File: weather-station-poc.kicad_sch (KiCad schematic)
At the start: 0 parts

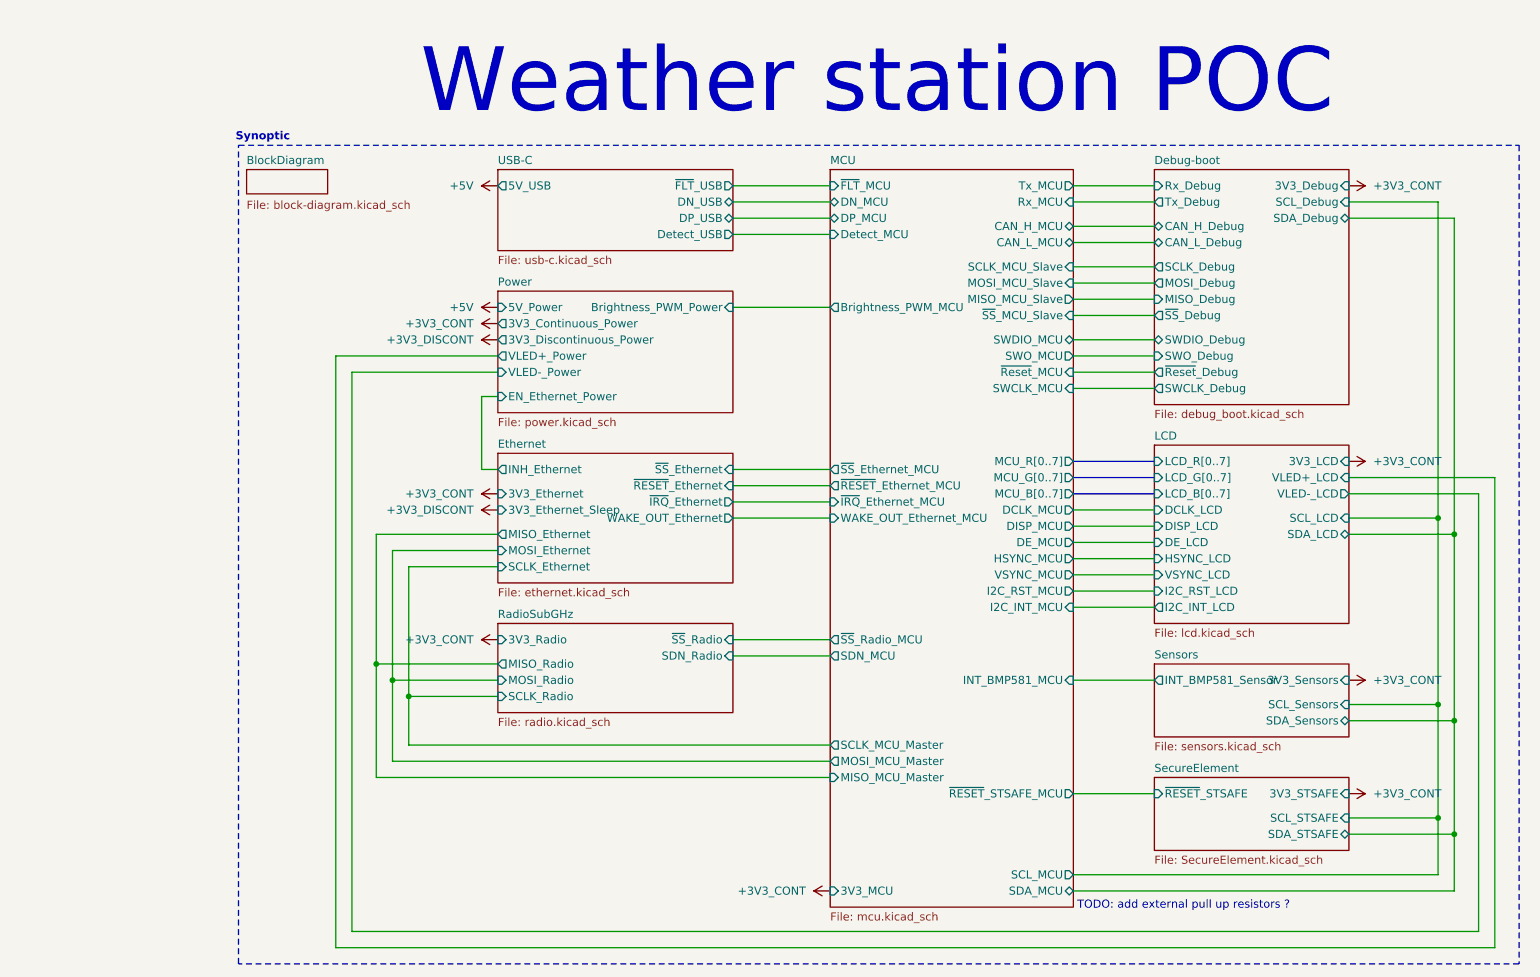
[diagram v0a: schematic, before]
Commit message: Remove Ethernet part, critical error, LAN8651 is 10BASE-T1S !
10BASE-T1S is not suitable with RJ45 connector and not connectable to computer
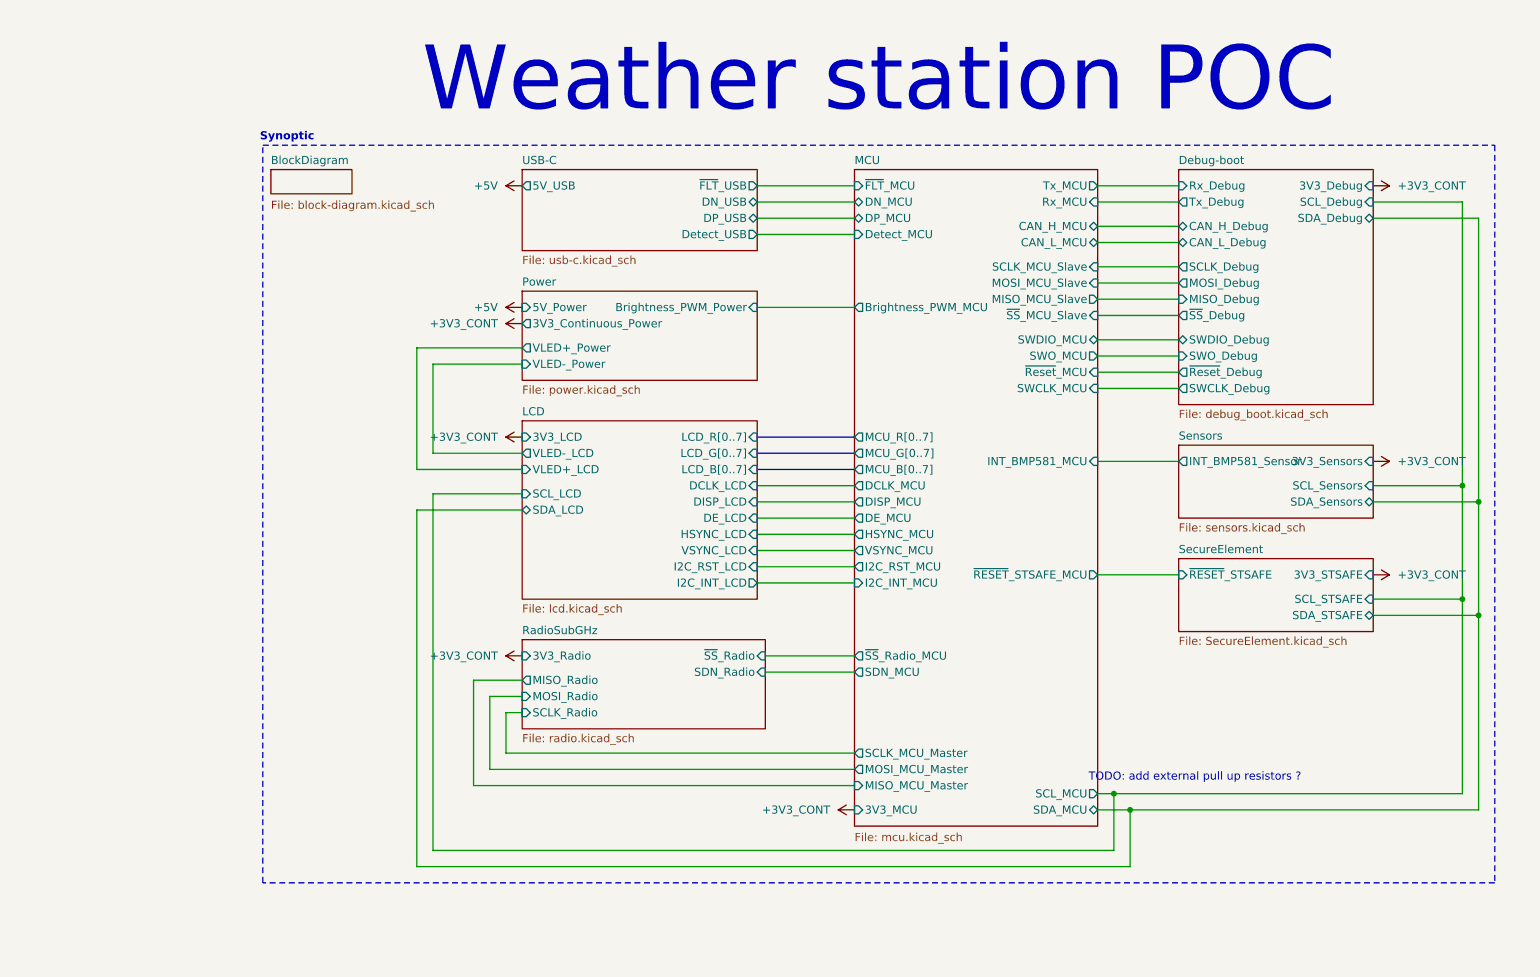
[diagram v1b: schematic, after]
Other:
- removed sheet Ethernet
- sheet MCU ports: added none; removed WAKE_OUT_Ethernet_MCU, ~{IRQ}_Ethernet_MCU, ~{RESET}_Ethernet_MCU, ~{SS}_Ethernet_MCU
- sheet Power ports: added none; removed 3V3_Discontinuous_Power, EN_Ethernet_Power

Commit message: Reorder components number
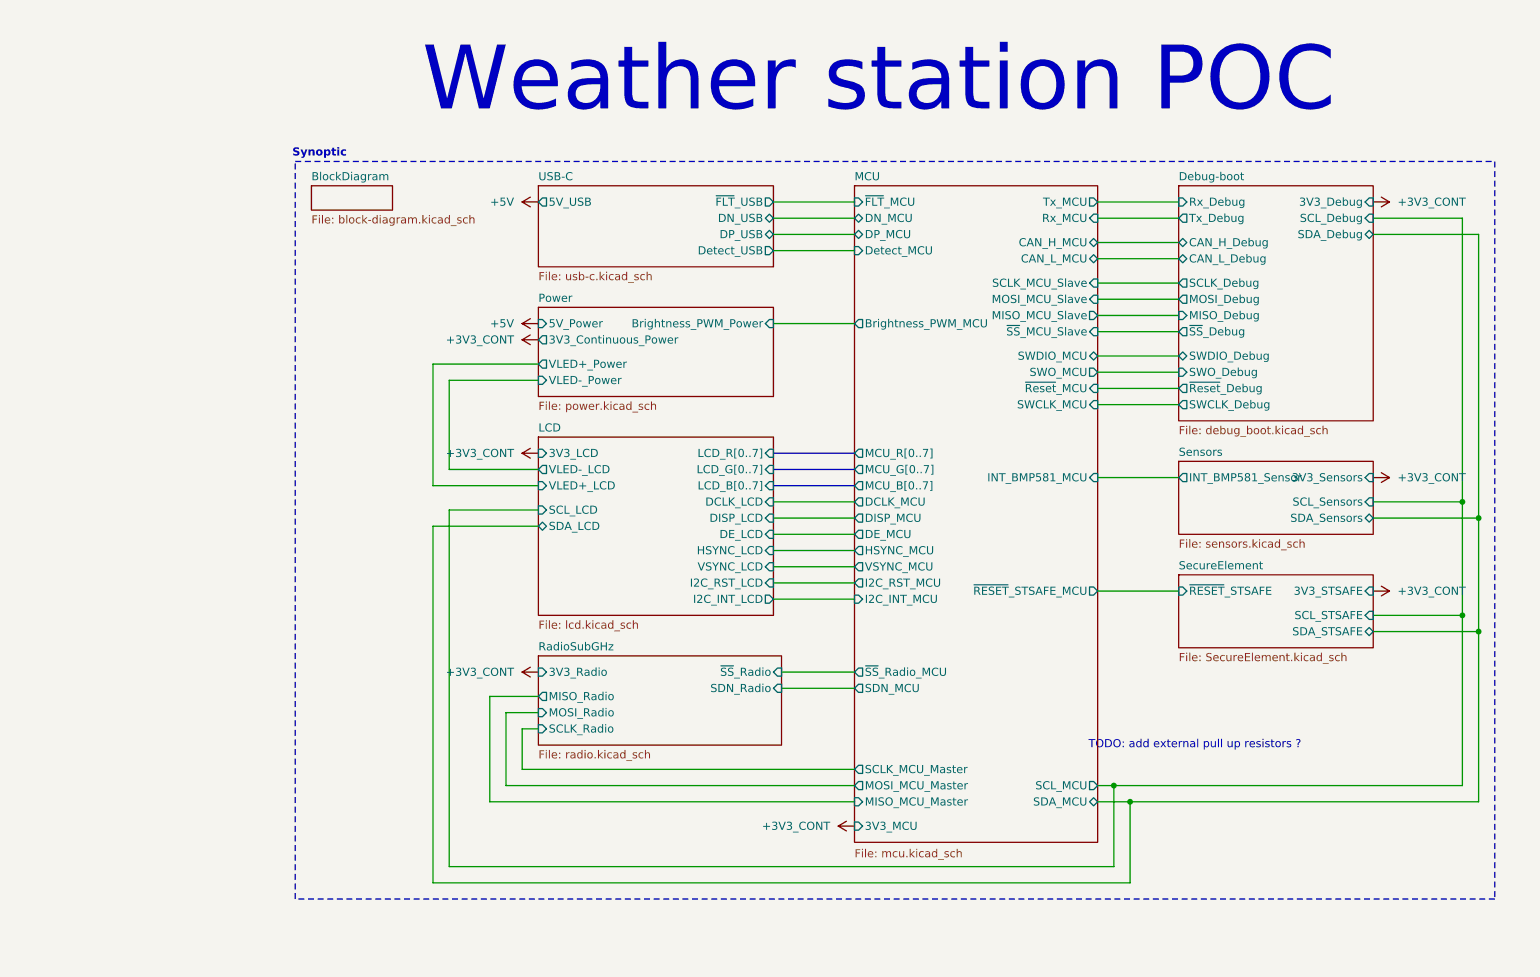
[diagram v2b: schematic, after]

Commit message: Modify USB data signals name to trace diff pairs
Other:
- sheet MCU ports: added MCU_DN, MCU_DP; removed DN_MCU, DP_MCU
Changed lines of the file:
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@@
-			)
-		)
-		(pin "DN_MCU" bidirectional
-			(at 144.78 44.45 180)
-			(effects
-				(font
-					(size 1.27 1.27)
-				)
-				(justify left)
-			)
-		)
-		(pin "DP_MCU" bidirectional
-			(at 144.78 46.99 180)
-			(effects
-				(font
-					(size 1.27 1.27)
-				)
-				(justify left)
 			)
 		)
@@
 			)
 		)
+		(pin "MCU_DN" bidirectional
+			(at 144.78 44.45 180)
+			(effects
+				(font
+					(size 1.27 1.27)
+				)
+				(justify left)
+			)
+		)
+		(pin "MCU_DP" bidirectional
+			(at 144.78 46.99 180)
+			(effects
+				(font
+					(size 1.27 1.27)
+				)
+				(justify left)
+			)
+		)

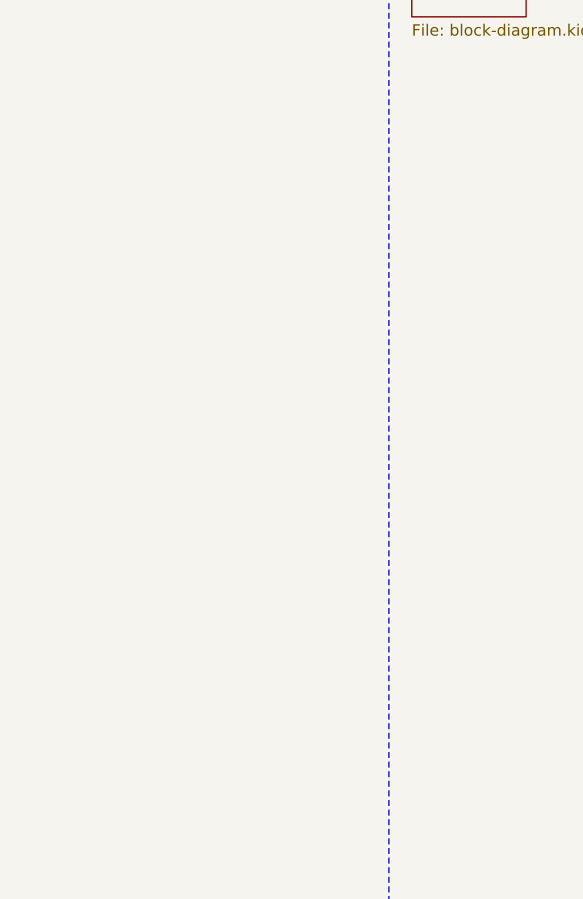
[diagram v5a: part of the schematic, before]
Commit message: Add mounting holes with pads in schematic and place it into pcb
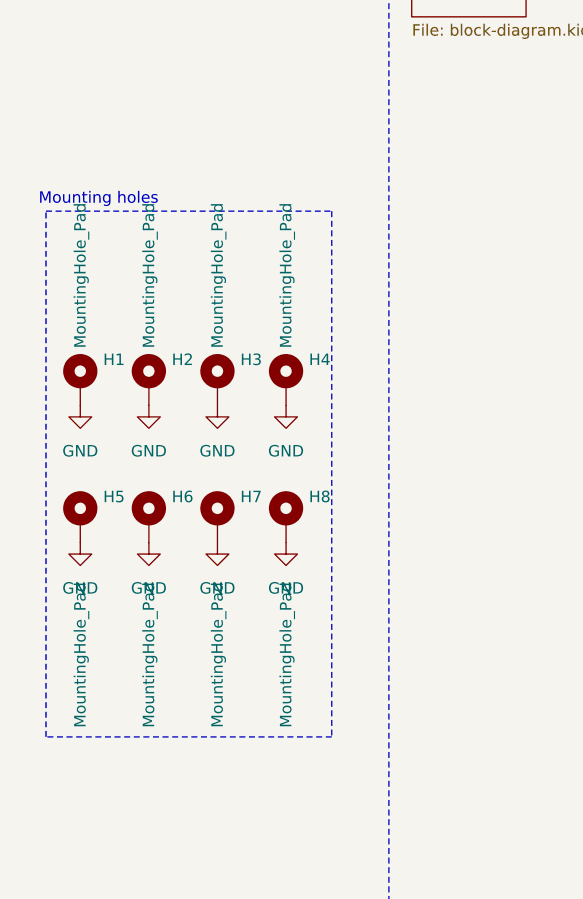
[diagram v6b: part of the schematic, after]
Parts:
- added H1, H2, H3, H4, H5, H6, H7, H8: MountingHole_Pad, MountingHole:MountingHole_3.5mm_Pad, symbol Mechanical:MountingHole_Pad
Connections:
- new net GND: H1.1, H2.1, H3.1, H4.1, H5.1, H6.1, H7.1, H8.1
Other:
- note added: "Mounting holes"

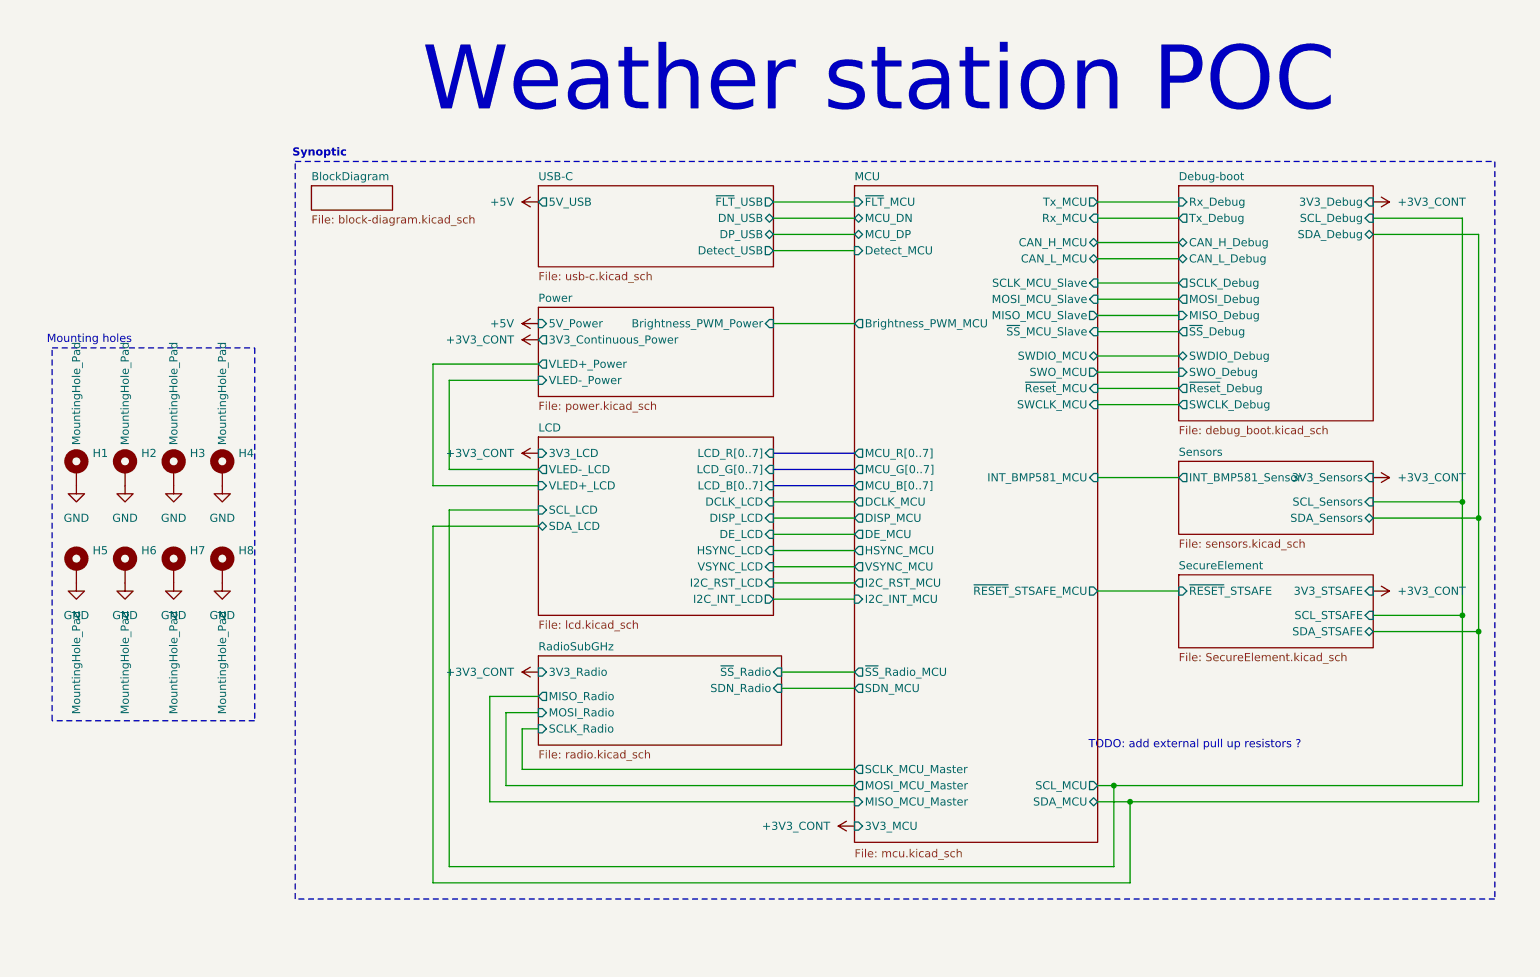
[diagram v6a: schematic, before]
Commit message: Use I2C for slave MCU for bootloader
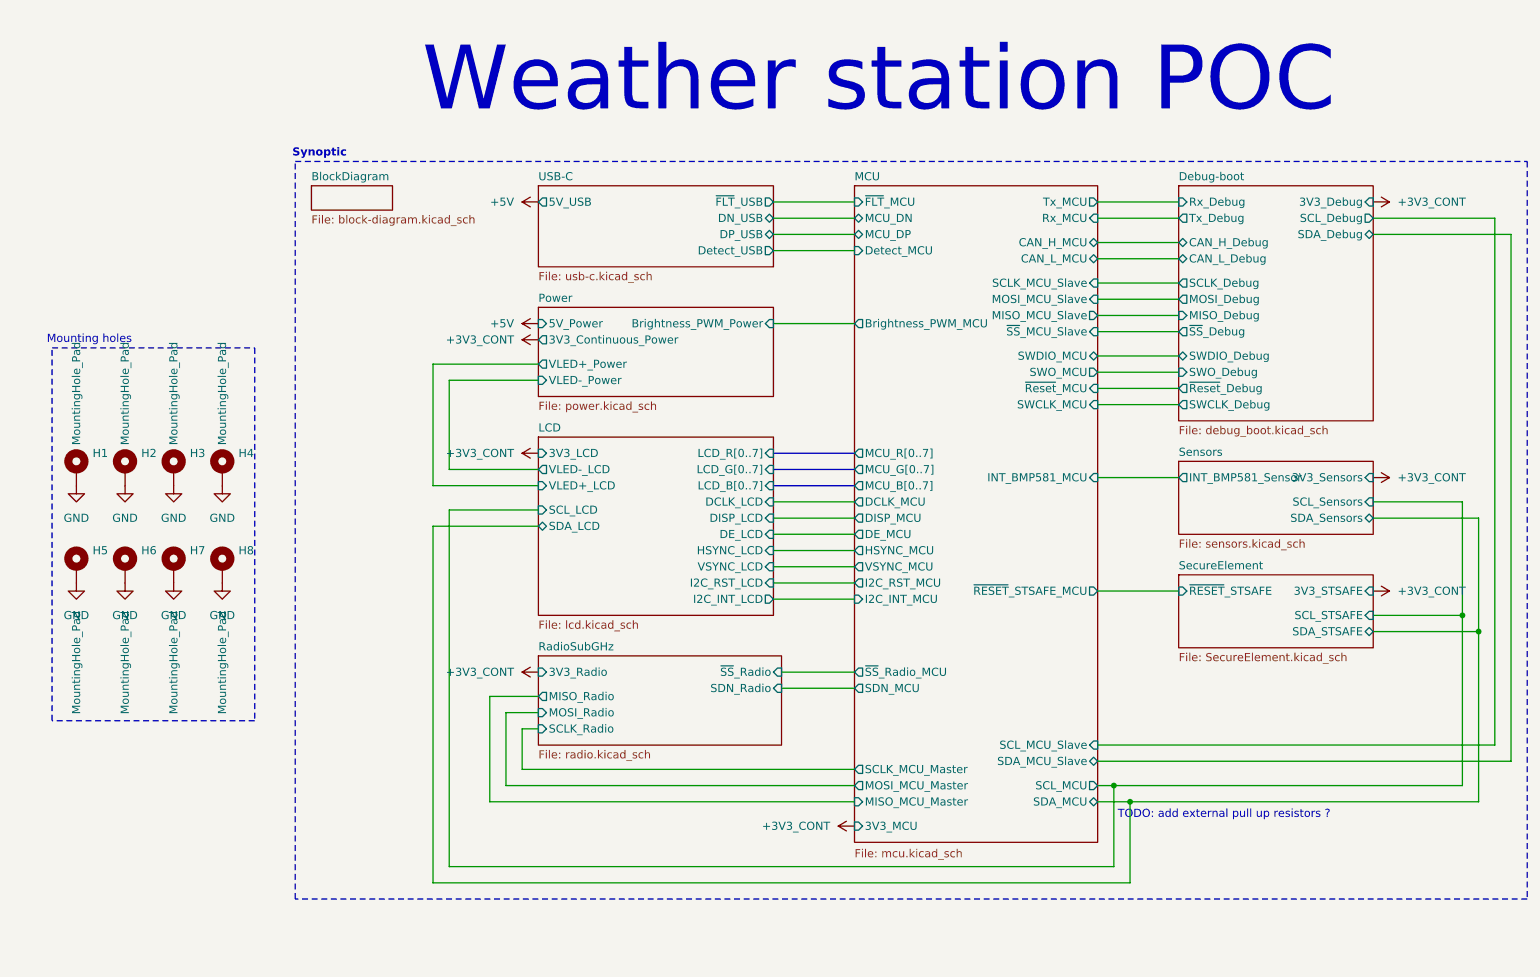
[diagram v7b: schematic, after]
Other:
- sheet MCU ports: added SCL_MCU_Slave, SDA_MCU_Slave; removed none
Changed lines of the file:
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@@
 	(rectangle
 		(start 57.15 35.56)
-		(end 245.11 151.13)
+		(end 250.19 151.13)
 		(stroke
 			(width 0)
@@
 	(text "TODO: add external pull up resistors ?"
 		(exclude_from_sim no)
-		(at 198.12 127 0)
+		(at 202.692 137.922 0)
 		(effects
 			(font
@@
 		(color 0 0 0 0)
 	)
-	(junction
-		(at 242.57 91.44)
-		(diameter 0)
-		(color 0 0 0 0)
-	)
-	(junction
-		(at 240.03 88.9)
-		(diameter 0)
-		(color 0 0 0 0)
-	)
 	(wire
 		(pts
@@
 	(wire
 		(pts
-			(xy 240.03 44.45) (xy 240.03 88.9)
-		)
-		(stroke
-			(width 0)
-			(type default)
-		)
-	)
-	(wire
-		(pts
 			(xy 182.88 71.12) (xy 195.58 71.12)
 		)
@@
 	(wire
 		(pts
-			(xy 226.06 46.99) (xy 242.57 46.99)
+			(xy 81.28 69.85) (xy 81.28 83.82)
 		)
 		(stroke
@@
 	(wire
 		(pts
-			(xy 81.28 69.85) (xy 81.28 83.82)
+			(xy 182.88 50.8) (xy 195.58 50.8)
 		)
 		(stroke
@@
 	(wire
 		(pts
-			(xy 182.88 50.8) (xy 195.58 50.8)
+			(xy 247.65 129.54) (xy 247.65 46.99)
 		)
 		(stroke
@@
 	(wire
 		(pts
+			(xy 182.88 129.54) (xy 247.65 129.54)
+		)
+		(stroke
+			(width 0)
+			(type default)
+		)
+	)
+	(wire
+		(pts
 			(xy 182.88 59.69) (xy 195.58 59.69)
 		)
@@
 	(wire
 		(pts
-			(xy 242.57 46.99) (xy 242.57 91.44)
+			(xy 245.11 127) (xy 182.88 127)
 		)
 		(stroke
@@
 	(wire
 		(pts
+			(xy 247.65 46.99) (xy 226.06 46.99)
+		)
+		(stroke
+			(width 0)
+			(type default)
+		)
+	)
+	(wire
+		(pts
 			(xy 133.35 115.57) (xy 144.78 115.57)
 		)
@@
 	(wire
 		(pts
-			(xy 226.06 44.45) (xy 240.03 44.45)
+			(xy 78.74 148.59) (xy 78.74 92.71)
 		)
 		(stroke
@@
 	(wire
 		(pts
-			(xy 78.74 148.59) (xy 78.74 92.71)
+			(xy 245.11 44.45) (xy 245.11 127)
 		)
 		(stroke
@@
 	(wire
 		(pts
+			(xy 226.06 44.45) (xy 245.11 44.45)
+		)
+		(stroke
+			(width 0)
+			(type default)
+		)
+	)
+	(wire
+		(pts
 			(xy 240.03 88.9) (xy 240.03 106.68)
 		)
@@
 			)
 		)
+		(pin "SCL_MCU_Slave" input
+			(at 182.88 127 0)
+			(effects
+				(font
+					(size 1.27 1.27)
+				)
+				(justify right)
+			)
+		)
+		(pin "SDA_MCU_Slave" bidirectional
+			(at 182.88 129.54 0)
+			(effects
+				(font
+					(size 1.27 1.27)
+				)
+				(justify right)
+			)
+		)
 		(instances
 			(project "weather-station-poc"
@@
 			)
 		)
-		(pin "SCL_Debug" input
-			(at 226.06 44.45 0)
-			(effects
-				(font
-					(size 1.27 1.27)
-				)
-				(justify right)
-			)
-		)
 		(pin "CAN_H_Debug" bidirectional
 			(at 195.58 48.26 180)
@@
 			)
 		)
+		(pin "SCL_Debug" output
+			(at 226.06 44.45 0)
+			(effects
+				(font
+					(size 1.27 1.27)
+				)
+				(justify right)
+			)
+		)
